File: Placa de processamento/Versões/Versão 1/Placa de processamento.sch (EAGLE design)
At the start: 12 parts

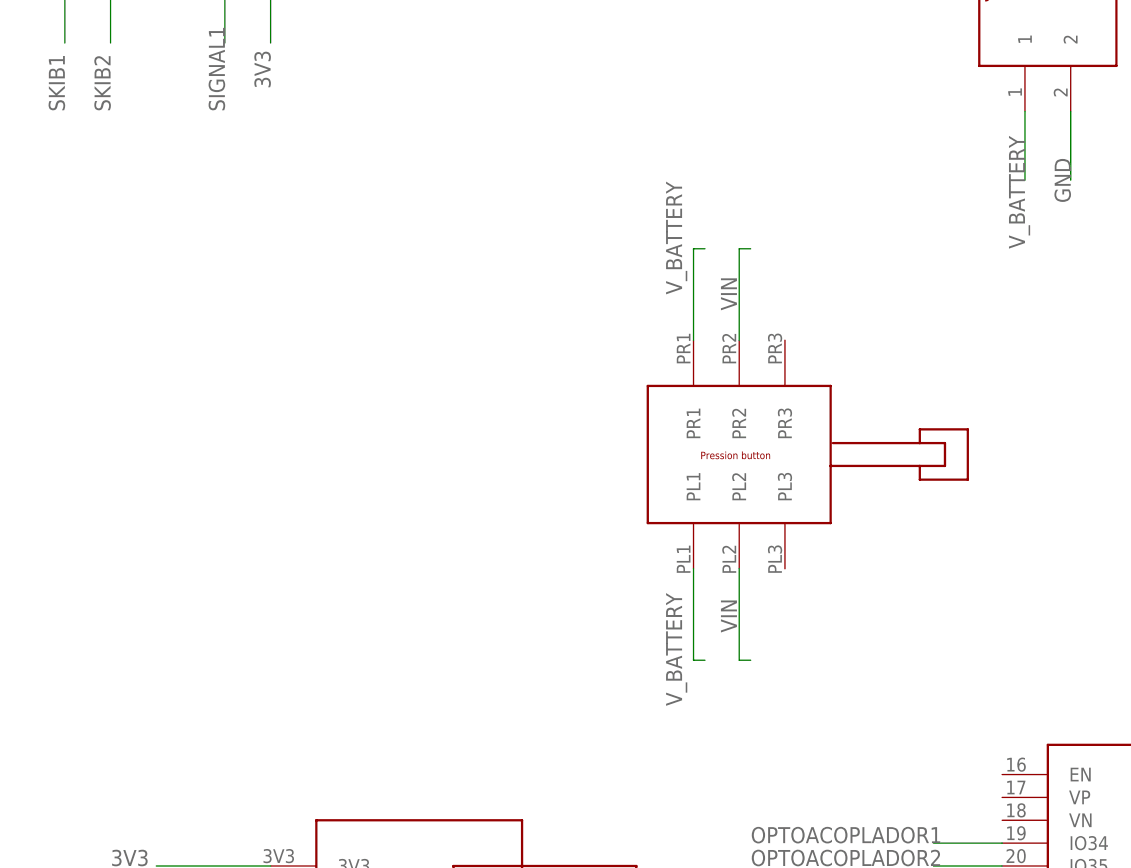
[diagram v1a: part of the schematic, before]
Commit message: FIX: consertando chave de acionamento
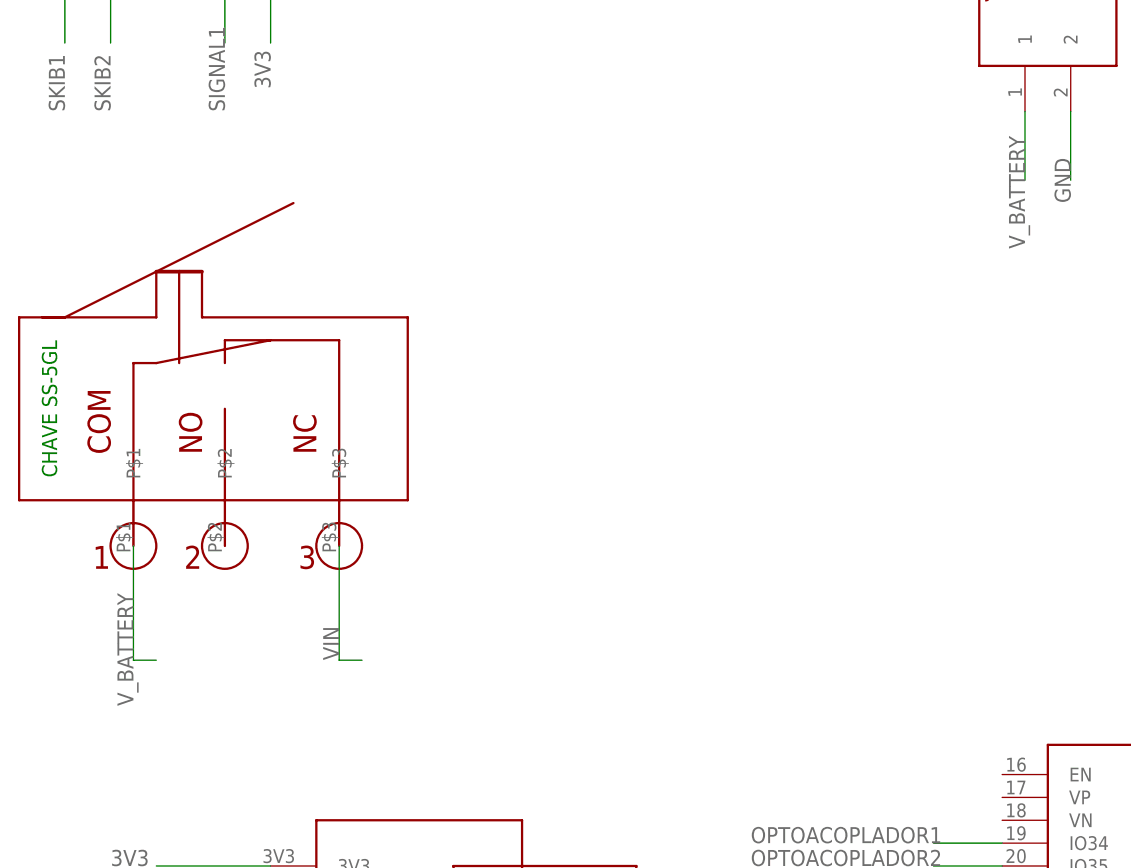
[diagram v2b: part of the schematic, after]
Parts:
- removed U$1: PRESSION_BUTTON, CRD:PRESSION_BUTTON
- added U$11: CHAVE_SS-5GL, CRD:CHAVE_SS-5GL
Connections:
- net VIN: now also U$11.P$3; no longer U$1.PL2, U$1.PR2
- net V_BATTERY: now also U$11.P$1; no longer U$1.PL1, U$1.PR1
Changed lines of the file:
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@@
 </classes>
 <parts>
-<part name="U$1" library="CRD" library_urn="urn:adsk.eagle:library:39051337" deviceset="PRESSION_BUTTON" device="" package3d_urn="urn:adsk.eagle:package:43483815/3" override_package3d_urn="urn:adsk.eagle:package:43483815/4" override_package_urn="urn:adsk.eagle:footprint:43483813/3"/>
 <part name="U$2" library="CRD" library_urn="urn:adsk.eagle:library:39051337" deviceset="MICROSD_SMALL_READER" device="" package3d_urn="urn:adsk.eagle:package:44017969/2" override_package3d_urn="urn:adsk.eagle:package:44017969/3" override_package_urn="urn:adsk.eagle:footprint:44017967/2"/>
 <part name="U$3" library="CRD" library_urn="urn:adsk.eagle:library:39051337" deviceset="JST2.54X2P" device="" package3d_urn="urn:adsk.eagle:package:39191967/2"/>
@@
 <part name="U$6" library="CRD" library_urn="urn:adsk.eagle:library:39051337" deviceset="JST2.54X2P" device="" package3d_urn="urn:adsk.eagle:package:39191967/2"/>
 <part name="U$7" library="CRD" library_urn="urn:adsk.eagle:library:39051337" deviceset="GPS_MODULE" device="" package3d_urn="urn:adsk.eagle:package:39608400/5" override_package3d_urn="urn:adsk.eagle:package:49474690/2" override_package_urn="urn:adsk.eagle:footprint:39608398/5"/>
-<part name="U$8" library="CRD" library_urn="urn:adsk.eagle:library:39051337" deviceset="E22-400T30D" device="" package3d_urn="urn:adsk.eagle:package:40965099/4"/>
-<part name="U$9" library="ESP32-DEVKITV1" library_urn="urn:adsk.eagle:library:44018017" deviceset="ESP32DEVKITV1" device="" package3d_urn="urn:adsk.eagle:package:44018021/1"/>
-<part name="IC1" library="v-reg" library_urn="urn:adsk.eagle:library:409" deviceset="78XXL" device="" package3d_urn="urn:adsk.eagle:package:30361/1" override_package3d_urn="urn:adsk.eagle:package:49474688/2" override_package_urn="urn:adsk.eagle:footprint:30303/1"/>
+<part name="U$8" library="CRD" library_urn="urn:adsk.eagle:library:39051337" deviceset="E22-400T30D" device="" package3d_urn="urn:adsk.eagle:package:40965099/4" override_package3d_urn="urn:adsk.eagle:package:40965099/7" override_package_urn="urn:adsk.eagle:footprint:40965097/4"/>
+<part name="U$9" library="ESP32-DEVKITV1" library_urn="urn:adsk.eagle:library:44018017" deviceset="ESP32DEVKITV1" device="" package3d_urn="urn:adsk.eagle:package:44018021/1" override_package3d_urn="urn:adsk.eagle:package:44018021/5" override_package_urn="urn:adsk.eagle:footprint:44018019/1"/>
+<part name="IC1" library="v-reg" library_urn="urn:adsk.eagle:library:409" deviceset="78XXL" device="" package3d_urn="urn:adsk.eagle:package:30361/1" override_package3d_urn="urn:adsk.eagle:package:49481284/2" override_package_urn="urn:adsk.eagle:footprint:30303/1"/>
 <part name="U$10" library="CRD" library_urn="urn:adsk.eagle:library:39051337" deviceset="JST2.54X2P" device="" package3d_urn="urn:adsk.eagle:package:39191967/2"/>
 <part name="SP1" library="buzzer" library_urn="urn:adsk.eagle:library:113" deviceset="AL11P" device="" package3d_urn="urn:adsk.eagle:package:5308/1" override_package3d_urn="urn:adsk.eagle:package:49474686/2" override_package_urn="urn:adsk.eagle:footprint:5250/1"/>
+<part name="U$11" library="CRD" library_urn="urn:adsk.eagle:library:39051337" deviceset="CHAVE_SS-5GL" device="" package3d_urn="urn:adsk.eagle:package:45208058/14"/>
 </parts>
 <sheets>
@@
 </plain>
 <instances>
-<instance part="U$1" gate="G$1" x="17.78" y="71.12" smashed="yes"/>
 <instance part="U$2" gate="G$1" x="-35.56" y="7.62" smashed="yes"/>
 <instance part="U$3" gate="G$1" x="45.72" y="119.38" smashed="yes"/>
@@
 <attribute name="VALUE" x="176.53" y="111.125" size="1.778" layer="96"/>
 </instance>
+<instance part="U$11" gate="G$1" x="-45.72" y="73.66" smashed="yes"/>
 </instances>
 <busses>
@@
 </segment>
 <segment>
-<pinref part="U$1" gate="G$1" pin="PL1"/>
-<wire x1="6.35" y1="58.42" x2="6.35" y2="48.26" width="0.1524" layer="91"/>
-<wire x1="6.35" y1="48.26" x2="7.62" y2="48.26" width="0.1524" layer="91"/>
-<label x="5.08" y="43.18" size="1.778" layer="95" rot="R90"/>
-</segment>
-<segment>
-<pinref part="U$1" gate="G$1" pin="PR1"/>
-<wire x1="6.35" y1="83.82" x2="6.35" y2="93.98" width="0.1524" layer="91"/>
-<wire x1="6.35" y1="93.98" x2="7.62" y2="93.98" width="0.1524" layer="91"/>
-<label x="5.08" y="88.9" size="1.778" layer="95" rot="R90"/>
+<pinref part="U$11" gate="G$1" pin="P$1"/>
+<wire x1="-55.88" y1="60.96" x2="-55.88" y2="48.26" width="0.1524" layer="91"/>
+<wire x1="-55.88" y1="48.26" x2="-53.34" y2="48.26" width="0.1524" layer="91"/>
+<label x="-55.88" y="43.18" size="1.778" layer="95" rot="R90"/>
 </segment>
 </net>
@@
 </segment>
 <segment>
-<pinref part="U$1" gate="G$1" pin="PL2"/>
-<wire x1="11.43" y1="58.42" x2="11.43" y2="48.26" width="0.1524" layer="91"/>
-<wire x1="11.43" y1="48.26" x2="12.7" y2="48.26" width="0.1524" layer="91"/>
-<label x="9.398" y="55.118" size="1.778" layer="95" rot="R270"/>
-</segment>
-<segment>
-<pinref part="U$1" gate="G$1" pin="PR2"/>
-<wire x1="11.43" y1="83.82" x2="11.43" y2="93.98" width="0.1524" layer="91"/>
-<wire x1="11.43" y1="93.98" x2="12.7" y2="93.98" width="0.1524" layer="91"/>
-<label x="11.176" y="87.122" size="1.778" layer="95" rot="R90"/>
-</segment>
-</net>
+<pinref part="U$11" gate="G$1" pin="P$3"/>
+<wire x1="-33.02" y1="60.96" x2="-33.02" y2="48.26" width="0.1524" layer="91"/>
+<wire x1="-33.02" y1="48.26" x2="-30.48" y2="48.26" width="0.1524" layer="91"/>
+<label x="-33.02" y="48.26" size="1.778" layer="95" rot="R90"/>
+</segment>
+</net>

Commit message: atualização placas
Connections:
- net 5V: now also U$9.VIN
- net VIN: no longer U$9.VIN
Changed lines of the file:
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@@
 <drawing>
 <settings>
-<setting alwaysvectorfont="no"/>
+<setting alwaysvectorfont="yes"/>
 <setting verticaltext="up"/>
 </settings>
@@
 <net name="VIN" class="0">
 <segment>
-<pinref part="U$9" gate="G$1" pin="VIN"/>
-<wire x1="40.64" y1="0" x2="33.02" y2="0" width="0.1524" layer="91"/>
-<label x="25.4" y="0" size="1.778" layer="95"/>
-</segment>
-<segment>
 <pinref part="IC1" gate="A" pin="IN"/>
 <wire x1="137.16" y1="73.66" x2="147.32" y2="73.66" width="0.1524" layer="91"/>
@@
 <label x="91.44" y="48.26" size="1.778" layer="95"/>
 </segment>
-</net>
+<segment>
+<pinref part="U$9" gate="G$1" pin="VIN"/>
+<wire x1="40.64" y1="0" x2="33.02" y2="0" width="0.1524" layer="91"/>
+<label x="25.4" y="0" size="1.778" layer="95"/>
+</segment>
+</net>

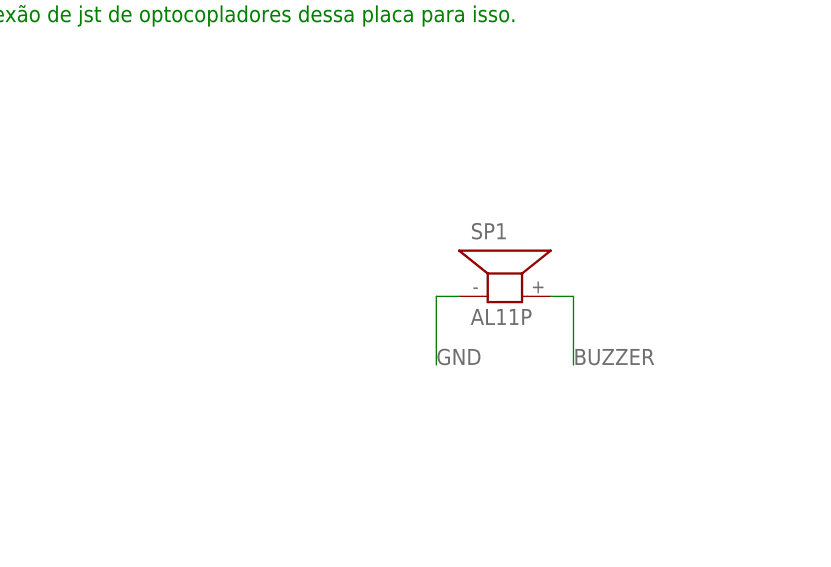
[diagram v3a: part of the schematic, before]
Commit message: CHORE: adicionando pads ovais na placa de processamento
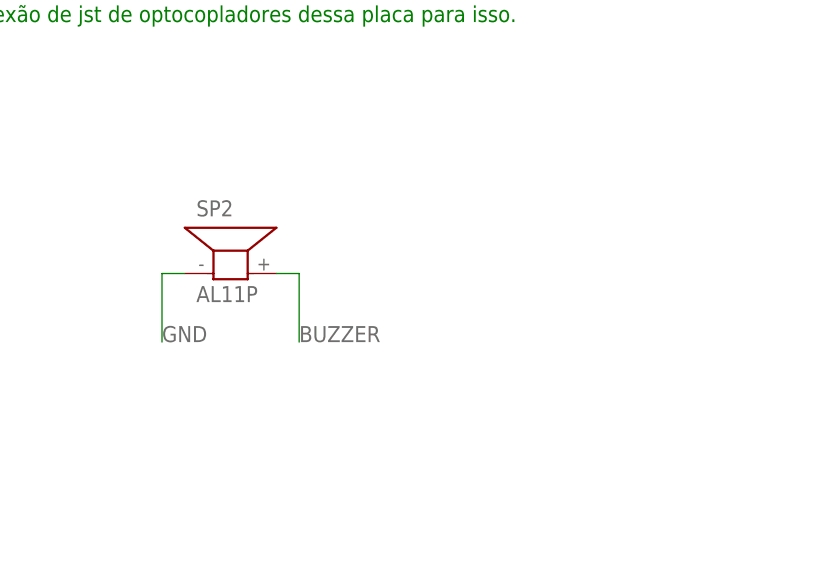
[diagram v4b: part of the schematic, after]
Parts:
- removed SP1: AL11P, buzzer:AL11P
- added SP2: AL11P, buzzer:AL11P
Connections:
- net BUZZER: now also SP2.2; no longer SP1.2
- net GND: now also SP2.1; no longer SP1.1
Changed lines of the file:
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@@
 <drawing>
 <settings>
-<setting alwaysvectorfont="yes"/>
+<setting alwaysvectorfont="no"/>
 <setting verticaltext="up"/>
 </settings>
@@
 </classes>
 <parts>
-<part name="U$2" library="CRD" library_urn="urn:adsk.eagle:library:39051337" deviceset="MICROSD_SMALL_READER" device="" package3d_urn="urn:adsk.eagle:package:44017969/2" override_package3d_urn="urn:adsk.eagle:package:44017969/3" override_package_urn="urn:adsk.eagle:footprint:44017967/2"/>
-<part name="U$3" library="CRD" library_urn="urn:adsk.eagle:library:39051337" deviceset="JST2.54X2P" device="" package3d_urn="urn:adsk.eagle:package:39191967/2"/>
-<part name="U$4" library="CRD" library_urn="urn:adsk.eagle:library:39051337" deviceset="JST2.54X2P" device="" package3d_urn="urn:adsk.eagle:package:39191967/2"/>
-<part name="U$5" library="CRD" library_urn="urn:adsk.eagle:library:39051337" deviceset="JST2.54X2P" device="" package3d_urn="urn:adsk.eagle:package:39191967/2"/>
-<part name="U$6" library="CRD" library_urn="urn:adsk.eagle:library:39051337" deviceset="JST2.54X2P" device="" package3d_urn="urn:adsk.eagle:package:39191967/2"/>
-<part name="U$7" library="CRD" library_urn="urn:adsk.eagle:library:39051337" deviceset="GPS_MODULE" device="" package3d_urn="urn:adsk.eagle:package:39608400/5" override_package3d_urn="urn:adsk.eagle:package:49474690/2" override_package_urn="urn:adsk.eagle:footprint:39608398/5"/>
-<part name="U$8" library="CRD" library_urn="urn:adsk.eagle:library:39051337" deviceset="E22-400T30D" device="" package3d_urn="urn:adsk.eagle:package:40965099/4" override_package3d_urn="urn:adsk.eagle:package:40965099/7" override_package_urn="urn:adsk.eagle:footprint:40965097/4"/>
-<part name="U$9" library="ESP32-DEVKITV1" library_urn="urn:adsk.eagle:library:44018017" deviceset="ESP32DEVKITV1" device="" package3d_urn="urn:adsk.eagle:package:44018021/1" override_package3d_urn="urn:adsk.eagle:package:44018021/5" override_package_urn="urn:adsk.eagle:footprint:44018019/1"/>
+<part name="U$2" library="CRD" library_urn="urn:adsk.eagle:library:39051337" deviceset="MICROSD_SMALL_READER" device="" package3d_urn="urn:adsk.eagle:package:44017969/2" override_package3d_urn="urn:adsk.eagle:package:44017969/3" override_package_urn="urn:adsk.eagle:footprint:44017967/2" override_locally_modified="yes"/>
+<part name="U$3" library="CRD" library_urn="urn:adsk.eagle:library:39051337" deviceset="JST2.54X2P" device="" package3d_urn="urn:adsk.eagle:package:39191967/4"/>
+<part name="U$4" library="CRD" library_urn="urn:adsk.eagle:library:39051337" deviceset="JST2.54X2P" device="" package3d_urn="urn:adsk.eagle:package:39191967/4"/>
+<part name="U$5" library="CRD" library_urn="urn:adsk.eagle:library:39051337" deviceset="JST2.54X2P" device="" package3d_urn="urn:adsk.eagle:package:39191967/4"/>
+<part name="U$6" library="CRD" library_urn="urn:adsk.eagle:library:39051337" deviceset="JST2.54X2P" device="" package3d_urn="urn:adsk.eagle:package:39191967/4"/>
+<part name="U$7" library="CRD" library_urn="urn:adsk.eagle:library:39051337" deviceset="GPS_MODULE" device="" package3d_urn="urn:adsk.eagle:package:39608400/7" override_package3d_urn="urn:adsk.eagle:package:49474690/2" override_package_urn="urn:adsk.eagle:footprint:39608398/5" override_locally_modified="yes"/>
+<part name="U$8" library="CRD" library_urn="urn:adsk.eagle:library:39051337" deviceset="E22-400T30D" device="" package3d_urn="urn:adsk.eagle:package:40965099/5" override_package3d_urn="urn:adsk.eagle:package:40965099/7" override_package_urn="urn:adsk.eagle:footprint:40965097/4" override_locally_modified="yes"/>
+<part name="U$9" library="ESP32-DEVKITV1" library_urn="urn:adsk.eagle:library:44018017" deviceset="ESP32DEVKITV1" device="" package3d_urn="urn:adsk.eagle:package:44018021/6"/>
 <part name="IC1" library="v-reg" library_urn="urn:adsk.eagle:library:409" deviceset="78XXL" device="" package3d_urn="urn:adsk.eagle:package:30361/1" override_package3d_urn="urn:adsk.eagle:package:49481284/2" override_package_urn="urn:adsk.eagle:footprint:30303/1"/>
-<part name="U$10" library="CRD" library_urn="urn:adsk.eagle:library:39051337" deviceset="JST2.54X2P" device="" package3d_urn="urn:adsk.eagle:package:39191967/2"/>
-<part name="SP1" library="buzzer" library_urn="urn:adsk.eagle:library:113" deviceset="AL11P" device="" package3d_urn="urn:adsk.eagle:package:5308/1" override_package3d_urn="urn:adsk.eagle:package:49474686/2" override_package_urn="urn:adsk.eagle:footprint:5250/1"/>
+<part name="U$10" library="CRD" library_urn="urn:adsk.eagle:library:39051337" deviceset="JST2.54X2P" device="" package3d_urn="urn:adsk.eagle:package:39191967/4"/>
 <part name="U$11" library="CRD" library_urn="urn:adsk.eagle:library:39051337" deviceset="CHAVE_SS-5GL" device="" package3d_urn="urn:adsk.eagle:package:45208058/14"/>
+<part name="SP2" library="buzzer" deviceset="AL11P" device="" package3d_urn="urn:adsk.eagle:package:5308/1"/>
 </parts>
 <sheets>
@@
 <instance part="U$6" gate="G$1" x="63.5" y="119.38" smashed="yes"/>
 <instance part="U$7" gate="G$1" x="124.46" y="22.86" smashed="yes"/>
-<instance part="U$8" gate="G$1" x="127" y="53.34" smashed="yes"/>
+<instance part="U$8" gate="LORA_E22400T30D" x="127" y="53.34" smashed="yes"/>
 <instance part="U$9" gate="G$1" x="58.42" y="22.86" smashed="yes" rot="R90">
 <attribute name="NAME" x="53.34" y="-3.81" size="1.27" layer="95" rot="R180"/>
@@
 </instance>
 <instance part="U$10" gate="G$1" x="86.36" y="119.38" smashed="yes"/>
-<instance part="SP1" gate="G$1" x="180.34" y="114.3" smashed="yes">
-<attribute name="NAME" x="176.53" y="120.65" size="1.778" layer="95"/>
-<attribute name="VALUE" x="176.53" y="111.125" size="1.778" layer="96"/>
+<instance part="U$11" gate="G$1" x="-45.72" y="73.66" smashed="yes"/>
+<instance part="SP2" gate="G$1" x="149.86" y="116.84" smashed="yes">
+<attribute name="NAME" x="146.05" y="123.19" size="1.778" layer="95"/>
+<attribute name="VALUE" x="146.05" y="113.665" size="1.778" layer="96"/>
 </instance>
-<instance part="U$11" gate="G$1" x="-45.72" y="73.66" smashed="yes"/>
 </instances>
 <busses>
@@
 </segment>
 <segment>
-<pinref part="U$8" gate="G$1" pin="GND"/>
+<pinref part="U$8" gate="LORA_E22400T30D" pin="GND"/>
 <wire x1="104.14" y1="45.72" x2="93.98" y2="45.72" width="0.1524" layer="91"/>
 <label x="88.9" y="45.72" size="1.778" layer="95"/>
@@
 </segment>
 <segment>
-<pinref part="SP1" gate="G$1" pin="1"/>
-<wire x1="175.26" y1="114.3" x2="172.72" y2="114.3" width="0.1524" layer="91"/>
-<wire x1="172.72" y1="114.3" x2="172.72" y2="106.68" width="0.1524" layer="91"/>
-<label x="172.72" y="106.68" size="1.778" layer="95"/>
+<pinref part="SP2" gate="G$1" pin="1"/>
+<wire x1="144.78" y1="116.84" x2="142.24" y2="116.84" width="0.1524" layer="91"/>
+<wire x1="142.24" y1="116.84" x2="142.24" y2="109.22" width="0.1524" layer="91"/>
+<label x="142.24" y="109.22" size="1.778" layer="95"/>
 </segment>
 </net>
@@
 </segment>
 <segment>
-<pinref part="U$8" gate="G$1" pin="M0"/>
+<pinref part="U$8" gate="LORA_E22400T30D" pin="M0"/>
 <wire x1="104.14" y1="60.96" x2="93.98" y2="60.96" width="0.1524" layer="91"/>
 <label x="91.44" y="60.96" size="1.778" layer="95"/>
@@
 </segment>
 <segment>
-<pinref part="U$8" gate="G$1" pin="M1"/>
+<pinref part="U$8" gate="LORA_E22400T30D" pin="M1"/>
 <wire x1="104.14" y1="58.42" x2="93.98" y2="58.42" width="0.1524" layer="91"/>
 <label x="91.44" y="58.42" size="1.778" layer="95"/>
@@
 </segment>
 <segment>
-<pinref part="U$8" gate="G$1" pin="TXD"/>
+<pinref part="U$8" gate="LORA_E22400T30D" pin="TXD"/>
 <wire x1="104.14" y1="53.34" x2="93.98" y2="53.34" width="0.1524" layer="91"/>
 <label x="88.9" y="53.34" size="1.778" layer="95"/>
@@
 </segment>
 <segment>
-<pinref part="U$8" gate="G$1" pin="RXD"/>
+<pinref part="U$8" gate="LORA_E22400T30D" pin="RXD"/>
 <wire x1="104.14" y1="55.88" x2="93.98" y2="55.88" width="0.1524" layer="91"/>
 <label x="88.9" y="55.88" size="1.778" layer="95"/>
@@
 <net name="N$3" class="0">
 <segment>
-<pinref part="U$8" gate="G$1" pin="AUX"/>
+<pinref part="U$8" gate="LORA_E22400T30D" pin="AUX"/>
 <wire x1="104.14" y1="50.8" x2="93.98" y2="50.8" width="0.1524" layer="91"/>
 </segment>
@@
 </segment>
 <segment>
-<pinref part="U$8" gate="G$1" pin="VCC"/>
+<pinref part="U$8" gate="LORA_E22400T30D" pin="VCC"/>
 <wire x1="104.14" y1="48.26" x2="93.98" y2="48.26" width="0.1524" layer="91"/>
 <label x="91.44" y="48.26" size="1.778" layer="95"/>
@@
 <net name="BUZZER" class="0">
 <segment>
-<pinref part="SP1" gate="G$1" pin="2"/>
-<wire x1="185.42" y1="114.3" x2="187.96" y2="114.3" width="0.1524" layer="91"/>
-<wire x1="187.96" y1="114.3" x2="187.96" y2="106.68" width="0.1524" layer="91"/>
-<label x="187.96" y="106.68" size="1.778" layer="95"/>
-</segment>
-<segment>
 <pinref part="U$9" gate="G$1" pin="IO27"/>
 <wire x1="40.64" y1="12.7" x2="33.02" y2="12.7" width="0.1524" layer="91"/>
 <label x="25.4" y="12.7" size="1.778" layer="95"/>
 </segment>
-</net>
+<segment>
+<pinref part="SP2" gate="G$1" pin="2"/>
+<wire x1="154.94" y1="116.84" x2="157.48" y2="116.84" width="0.1524" layer="91"/>
+<wire x1="157.48" y1="116.84" x2="157.48" y2="109.22" width="0.1524" layer="91"/>
+<label x="157.48" y="109.22" size="1.778" layer="95"/>
+</segment>
+</net>
